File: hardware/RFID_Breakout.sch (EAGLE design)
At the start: 5 parts, among them U1 RFID

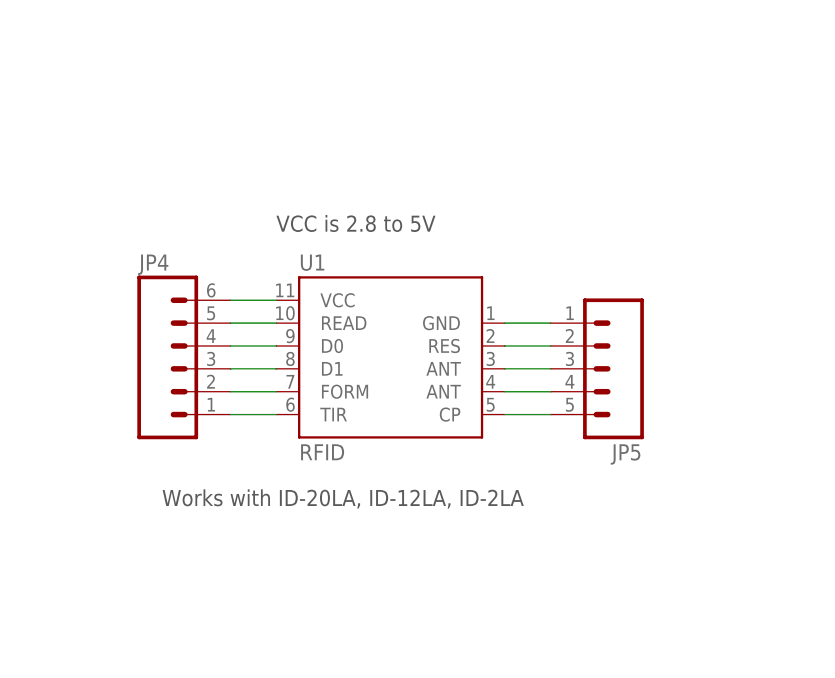
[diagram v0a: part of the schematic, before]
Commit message: Reversed layout to make labels visible when attached.
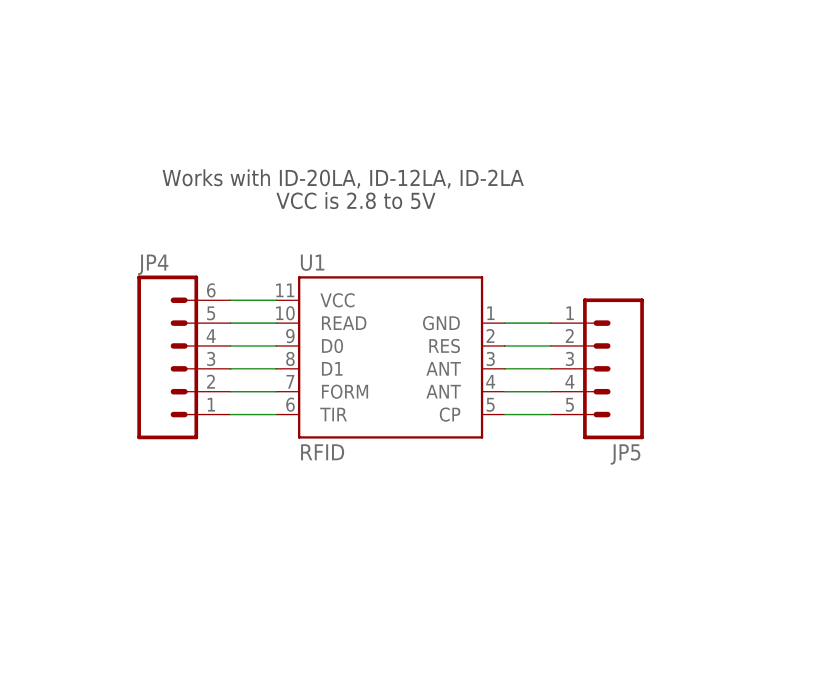
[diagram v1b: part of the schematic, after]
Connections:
- net GND renamed N$3
- net VCC renamed N$2
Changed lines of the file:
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@@
 <sheet>
 <plain>
-<text x="104.14" y="109.22" size="1.778" layer="97">VCC is 2.8 to 5V</text>
+<text x="104.14" y="111.76" size="1.778" layer="97">VCC is 2.8 to 5V</text>
 <text x="241.3" y="7.62" size="1.778" layer="97">v2.0</text>
 <text x="172.72" y="10.16" size="1.778" layer="97">N. Seidle</text>
-<text x="91.44" y="78.74" size="1.778" layer="97">Works with ID-20LA, ID-12LA, ID-2LA</text>
+<text x="91.44" y="114.3" size="1.778" layer="97">Works with ID-20LA, ID-12LA, ID-2LA</text>
 </plain>
 <instances>
@@
 </segment>
 </net>
-<net name="VCC" class="0">
+<net name="N$2" class="0">
 <segment>
+<pinref part="JP4" gate="G$1" pin="6"/>
 <pinref part="U1" gate="G$1" pin="VCC"/>
-<pinref part="JP4" gate="G$1" pin="6"/>
 <wire x1="104.14" y1="101.6" x2="99.06" y2="101.6" width="0.1524" layer="91"/>
 </segment>
 </net>
-<net name="GND" class="0">
+<net name="N$3" class="0">
 <segment>
+<pinref part="JP5" gate="G$1" pin="1"/>
 <pinref part="U1" gate="G$1" pin="GND"/>
-<pinref part="JP5" gate="G$1" pin="1"/>
 <wire x1="129.54" y1="99.06" x2="134.62" y2="99.06" width="0.1524" layer="91"/>
 </segment>

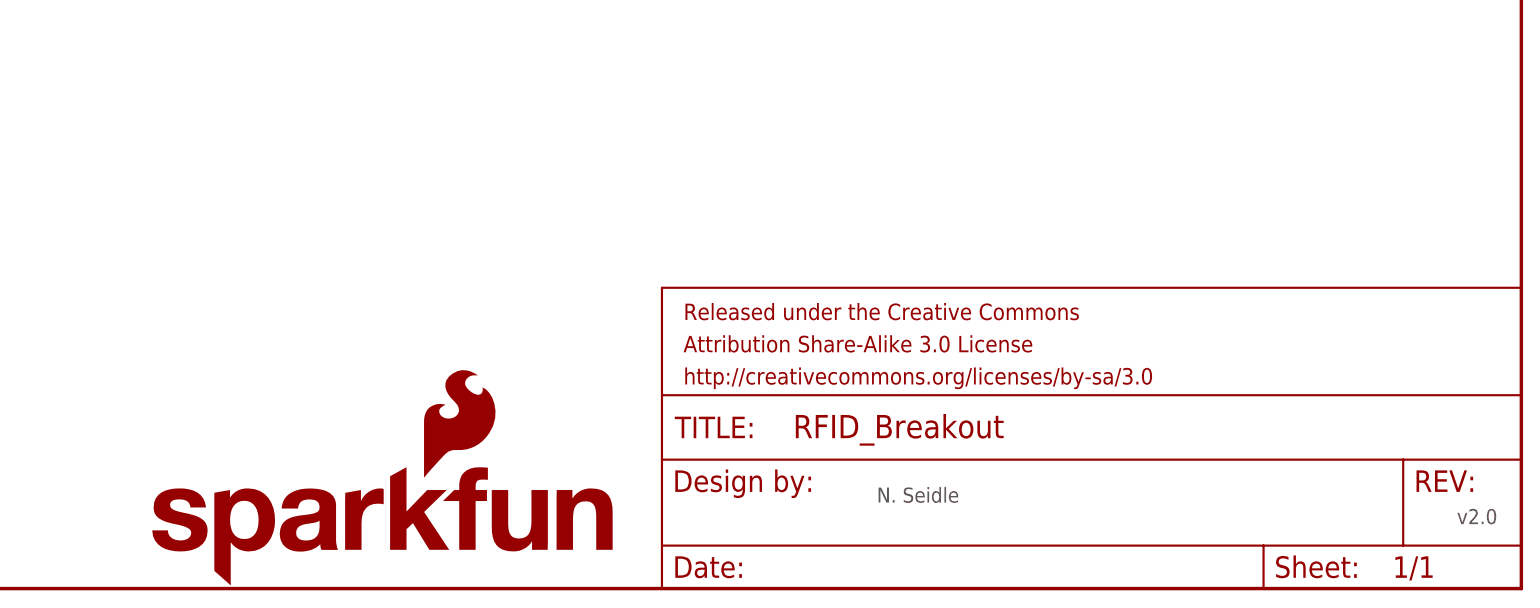
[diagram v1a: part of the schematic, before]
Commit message: Updating silkscreen to both sides, adding in OSHW logo, adding in bottom copper for version number
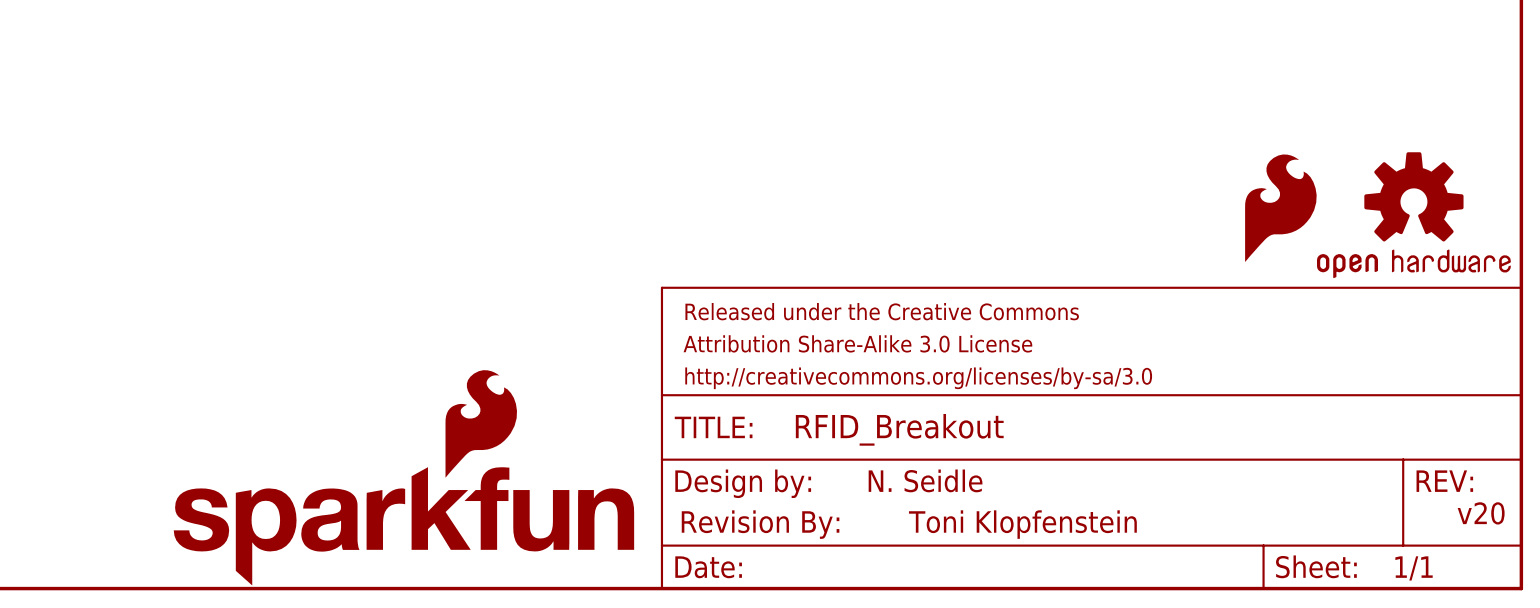
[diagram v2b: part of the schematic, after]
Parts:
- added LOGO1: SFE_LOGO_FLAME.1_INCH, SparkFun-Aesthetics:SFE_LOGO_FLAME.1_INCH
- added LOGO3: OSHW-LOGOS, SparkFun-Aesthetics:OSHW-LOGOS
- added U$1: REVISION, SparkFun-Aesthetics:REVISION
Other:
- note added: "Toni Klopfenstein"
- note added: "v20"
- note removed: "v2.0"
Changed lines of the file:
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@@
 <part name="JP4" library="SparkFun-Connectors" deviceset="M06" device="SIP"/>
 <part name="JP5" library="SparkFun-Connectors" deviceset="M05" device="PTH"/>
+<part name="LOGO3" library="SparkFun-Aesthetics" deviceset="OSHW-LOGO" device="S"/>
+<part name="U$1" library="SparkFun-Aesthetics" deviceset="REVISION" device=""/>
+<part name="LOGO1" library="SparkFun-Aesthetics" deviceset="SFE_LOGO_FLAME" device=".1_INCH"/>
 </parts>
 <sheets>
@@
 <plain>
 <text x="104.14" y="111.76" size="1.778" layer="97">VCC is 2.8 to 5V</text>
-<text x="241.3" y="7.62" size="1.778" layer="97">v2.0</text>
-<text x="172.72" y="10.16" size="1.778" layer="97">N. Seidle</text>
+<text x="241.3" y="7.62" size="2.54" layer="94">v20</text>
+<text x="171.45" y="11.43" size="2.54" layer="94">N. Seidle</text>
 <text x="91.44" y="114.3" size="1.778" layer="97">Works with ID-20LA, ID-12LA, ID-2LA</text>
+<text x="176.53" y="6.604" size="2.54" layer="94">Toni Klopfenstein</text>
 </plain>
 <instances>
 <instance part="U1" gate="G$1" x="116.84" y="96.52"/>
-<instance part="LOGO2" gate="G$1" x="86.36" y="0"/>
+<instance part="LOGO2" gate="G$1" x="88.9" y="0"/>
 <instance part="FRAME1" gate="G$1" x="0" y="0"/>
 <instance part="FRAME1" gate="G$2" x="147.32" y="0"/>
 <instance part="JP4" gate="G$1" x="93.98" y="93.98"/>
 <instance part="JP5" gate="G$1" x="142.24" y="93.98" rot="R180"/>
+<instance part="LOGO3" gate="G$1" x="236.22" y="45.72"/>
+<instance part="U$1" gate="G$1" x="149.352" y="6.604"/>
+<instance part="LOGO1" gate="G$1" x="215.9" y="38.1"/>
 </instances>
 <busses>
